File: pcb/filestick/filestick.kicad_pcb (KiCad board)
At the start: 4 copper layers, 88 x 54 mm, 106 parts, among them J1 USB_B_Micro, J2 DIN-5_180degree, J3 DIN-5_180degree, J4 Micro_SD_Card_Det2, J5 Conn_01x08_Pin, J6 Conn_01x09_Pin, J7 Conn_01x02_Pin, J8 Conn_02x08_Odd_Even, J9 Conn_01x02_Pin, Q1 2N7002, Q2 2N7002, Q3 2N7002, Q4 2N7002, Q5 2N7002, U1 ICE40UP5K-SG48ITR, U2 FT230XS, U3 SN65HVD75, U4 SN65HVD75, U5 AT25SF081-SSHD-X, U6 LD1117S33TR_SOT223, U7 LD1117S12TR_SOT223, U8 LMV324, X1 ASV-xxxMHz

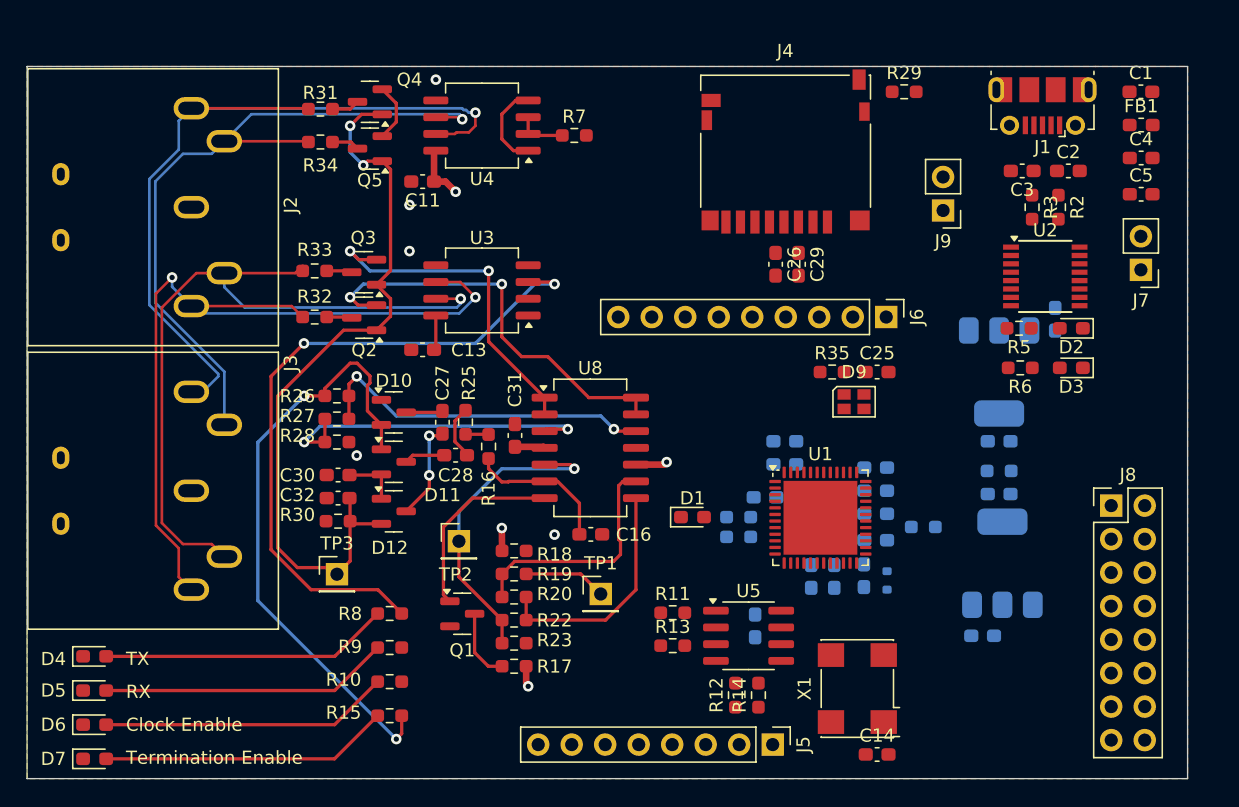
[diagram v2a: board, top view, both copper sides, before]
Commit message: Route the rest of the PCB
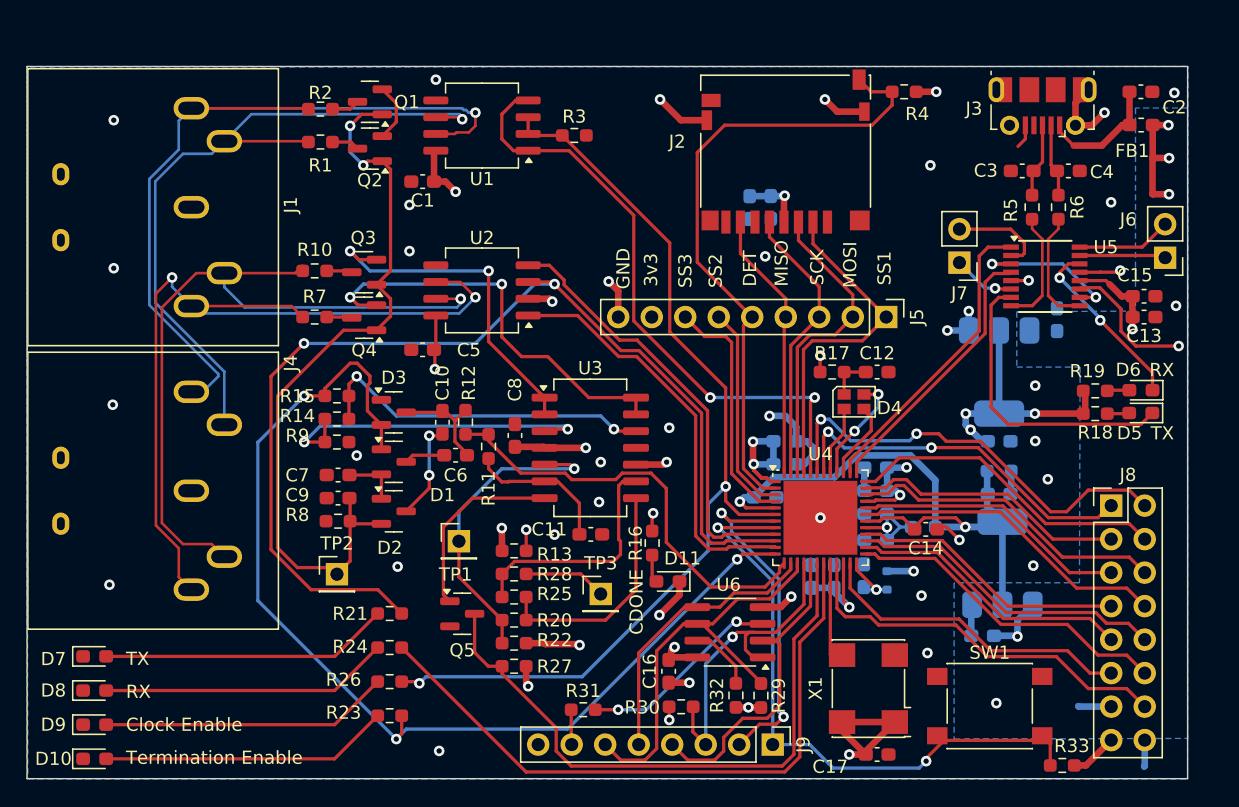
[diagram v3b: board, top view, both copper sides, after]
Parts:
- added C14: 100nF, Capacitor_SMD:C_0603_1608Metric_Pad1.08x0.95mm_HandSolder, F.Cu at (169.7, 111.6)
- added SW1: SW_Push, Button_Switch_SMD:SW_SPST_PTS645, F.Cu at (174.5, 125.0)
- C16: renamed from C15; moved to F.Cu
- C18: renamed from C29; moved to B.Cu
- C19: renamed from C26; moved to B.Cu
- R16: renamed from R4; moved to F.Cu
- R33: renamed from R1; moved to F.Cu
- moved R33 30.0 mm to (180.0, 129.5), turned to 180 degrees
- moved C13 12.1 mm to (186.2, 95.5), turned to 180 degrees
- moved R31 8.34 mm to (143.7, 125.3)
- moved C15 7.74 mm to (186.2, 93.9), turned to 180 degrees
- moved R19 7.48 mm to (182.5, 101.1)
- moved C16 7.41 mm to (150.2, 122.4)
- moved R30 7.16 mm to (151.1, 125.0)
- moved D6 7.07 mm to (186.0, 101.0)
- moved R16 6.85 mm to (148.9, 112.6), turned to -90 degrees
- moved R18 6.67 mm to (182.5, 102.8)
- moved D5 6.28 mm to (185.9, 102.8)
- moved C18 5.67 mm to (156.3, 87.2)
- moved D11 5.22 mm to (150.1, 115.5), turned to 180 degrees
- moved C19 4.33 mm to (157.9, 87.2)
- moved J7 4.14 mm to (172.2, 91.4)
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- renumbered C11 to C1, C27 to C10, C16 to C11, C25 to C12, C4 to C13, C5 to C15, C14 to C17, C1 to C2, C6 to C20, C24 to C21, C8 to C22, C20 to C23, C23 to C24, C17 to C25, C19 to C26, C12 to C27, C10 to C28, C22 to C29, C18 to C30, C7 to C31, C21 to C32, C9 to C33, C2 to C4, C13 to C5, C28 to C6, C30 to C7, C31 to C8, C32 to C9, D11 to D1, D7 to D10, D1 to D11, D8 to D12, D12 to D2, D10 to D3, D9 to D4, D3 to D5, D2 to D6, D4 to D7, D5 to D8, D6 to D9, J2 to J1, J4 to J2, J1 to J3, J3 to J4, J6 to J5, J7 to J6, J9 to J7, J5 to J9, Q4 to Q1, Q5 to Q2, Q2 to Q4, Q1 to Q5, R34 to R1, R33 to R10, R16 to R11, R25 to R12, R18 to R13, R27 to R14, R26 to R15, R35 to R17, R6 to R18, R5 to R19, R31 to R2, R22 to R20, R8 to R21, R23 to R22, R15 to R23, R9 to R24, R20 to R25, R10 to R26, R17 to R27, R19 to R28, R12 to R29, R7 to R3, R11 to R30, R13 to R31, R14 to R32, R24 to R34, R21 to R35, R29 to R4, R3 to R5, R2 to R6, R32 to R7, R30 to R8, R28 to R9, TP2 to TP1, TP3 to TP2, TP1 to TP3, U4 to U1, U3 to U2, U8 to U3, U1 to U4, U2 to U5, U5 to U6, U6 to U8
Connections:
- net Net-(U2-USBDM) renamed /USB-
- net Net-(U2-USBDP) renamed /USB+
- J8 pad 1: /GPIO_37 -> /GPIO_42
- J8 pad 10: /GPIO_25 -> /GPIO_27
- J8 pad 12: /GPIO_21 -> /GPIO_25
- J8 pad 14: GND -> /GPIO_21
- J8 pad 2: /GPIO_36 -> /GPIO_43
- J8 pad 4: /GPIO_34 -> /GPIO_36
- J8 pad 6: /GPIO_31 -> /GPIO_34
- J8 pad 8: /GPIO_27 -> /GPIO_31
- U4 pad 37: /GPIO_37 -> /UART_RX
- U4 pad 38: /UART_RX -> /UART_TX
- U4 pad 42: /UART_TX -> /GPIO_42
- U4 pad 43: /ECONET_CLKIO -> /GPIO_43
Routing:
- net +5V: track 2.28 -> 97.3 mm, vias 0 -> 5
- net +3V3: track 10.1 -> 97.2 mm, vias 4 -> 21
- net /ECONET_CLKEN: track 3.91 -> 73.8 mm, vias 0 -> 2
- net GND: track 0.00 -> 62.8 mm, vias 5 -> 43
- net /ECONET_RECEIVING: track 0.00 -> 50.0 mm
- net //SD_DETECT: track 0.00 -> 49.1 mm
- net +1V2: track 0.00 -> 47.8 mm, vias 0 -> 2
- net //CRESET: track 0.00 -> 47.8 mm, vias 0 -> 2
- net /COLLISION_DETECT: track 5.45 -> 47.7 mm
- net /ECONET_CLKIO: track 6.67 -> 46.7 mm, vias 0 -> 2
- net /ECONET_TERM_EN: track 46.6 -> 81.1 mm, vias 2 -> 3
- net /GPIO_43: track 0.00 -> 33.2 mm, vias 0 -> 2
- net /ECONET_TX: track 0.00 -> 32.9 mm
- net /CDONE: track 0.00 -> 32.7 mm, vias 0 -> 3
- net /FLASH_SCK: track 0.00 -> 32.7 mm
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- added copper zone on B.Cu, net +5V
- added copper zone on B.Cu, net GND
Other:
- board text added: "3v3"
- board text added: "CDONE"
- board text added: "DET"
- board text added: "GND"
- board text added: "MISO"
- board text added: "MOSI"
- board text added: "SCK"
- board text added: "SS1"
- board text added: "SS2"
- board text added: "SS3"

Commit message: Update kicad files to v9, turn micro-sd card slot the right way
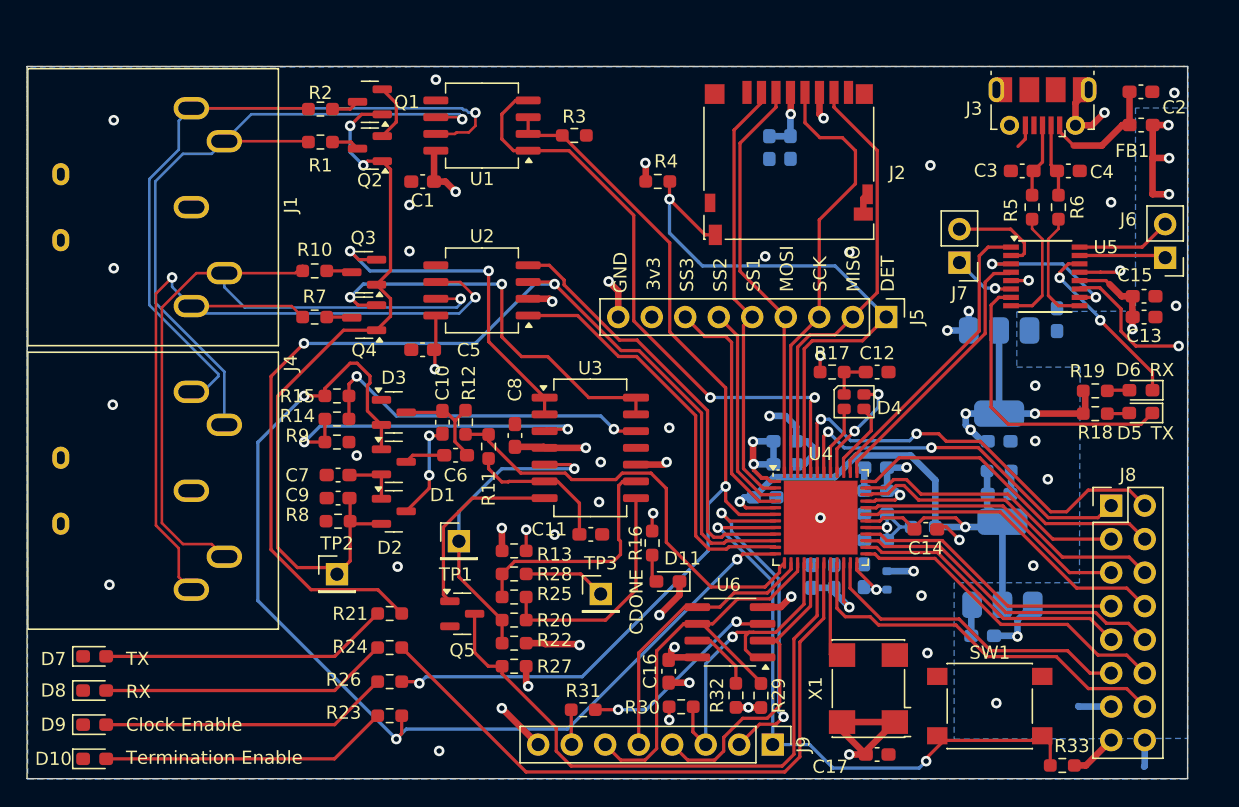
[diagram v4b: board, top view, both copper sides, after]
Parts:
- U1, U2: footprint Package_SO:SO-8_5.3x6.2mm_P1.27mm -> Package_SO:SOIC-8_5.3x6.2mm_P1.27mm
- moved R4 19.9 mm to (149.3, 85.2), turned to 180 degrees
- moved C19 4.78 mm to (159.4, 82.6)
- moved C18 4.78 mm to (157.8, 82.7)
- moved J2 0.90 mm to (159.3, 83.8), turned to 180 degrees
- turned C16 to -90 degrees
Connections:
- C16 pad 1: GND -> +3V3
- C16 pad 2: +3V3 -> GND
- J5 pad 1: /SD_CS -> //SD_DETECT
- J5 pad 2: /SD_MOSI -> /SD_MISO
- J5 pad 4: /SD_MISO -> /SD_MOSI
- J5 pad 5: //SD_DETECT -> /SD_CS
- U4 pad 2: //SD_DETECT -> /SD_CS
- U4 pad 45: /SD_CS -> //SD_DETECT
- U4 pad 46: /SD_MOSI -> /SD_MISO
- U4 pad 48: /SD_MISO -> /SD_MOSI
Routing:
- net /SD_MISO: track 20.5 -> 33.8 mm
- net /SD_SCK: track 21.4 -> 33.4 mm
- net /SD_MOSI: track 23.5 -> 31.4 mm
- net /SD_CS: track 26.1 -> 33.2 mm
- net //SD_DETECT: track 49.1 -> 44.2 mm, vias 0 -> 1
- net GND: track 62.8 -> 62.9 mm, vias 43 -> 44
